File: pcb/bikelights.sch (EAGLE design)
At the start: 8 parts, among them J1 COMPUTER-PERIPHERAL-POWERRA

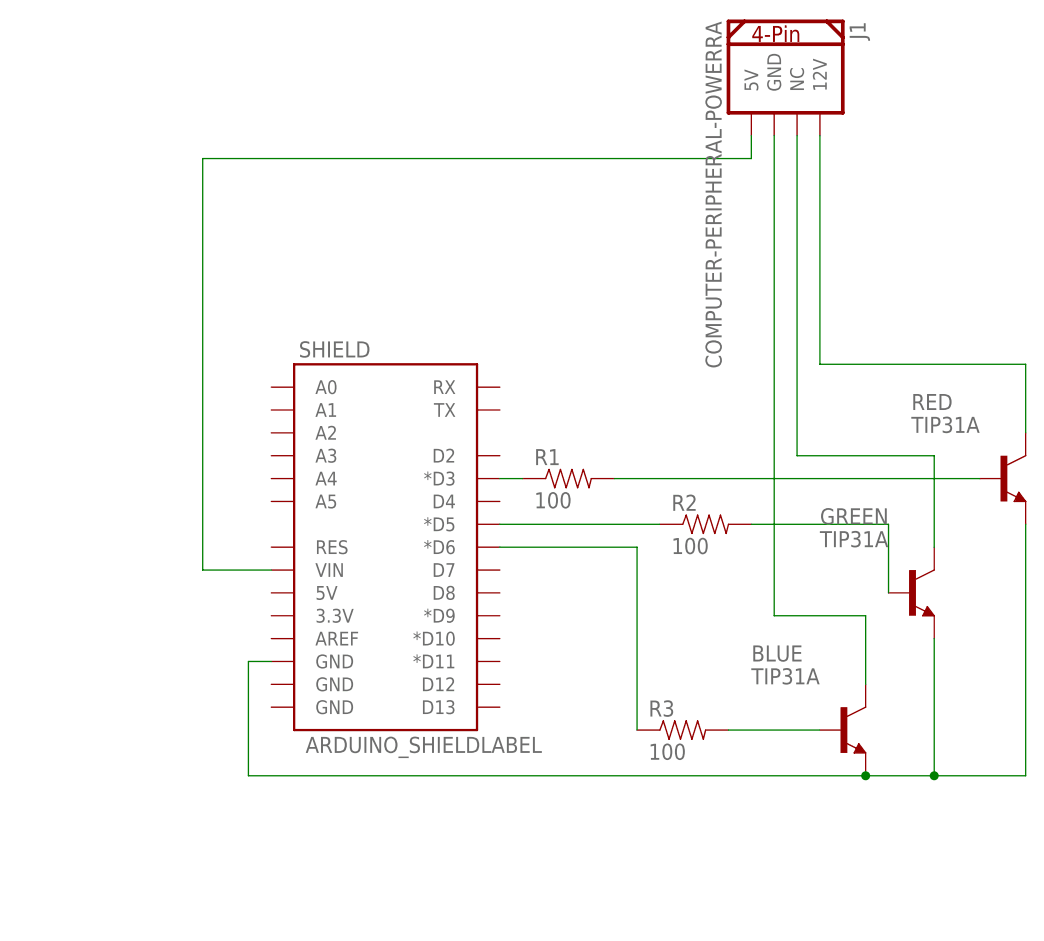
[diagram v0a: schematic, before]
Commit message: New PCB for blinkenthing B.
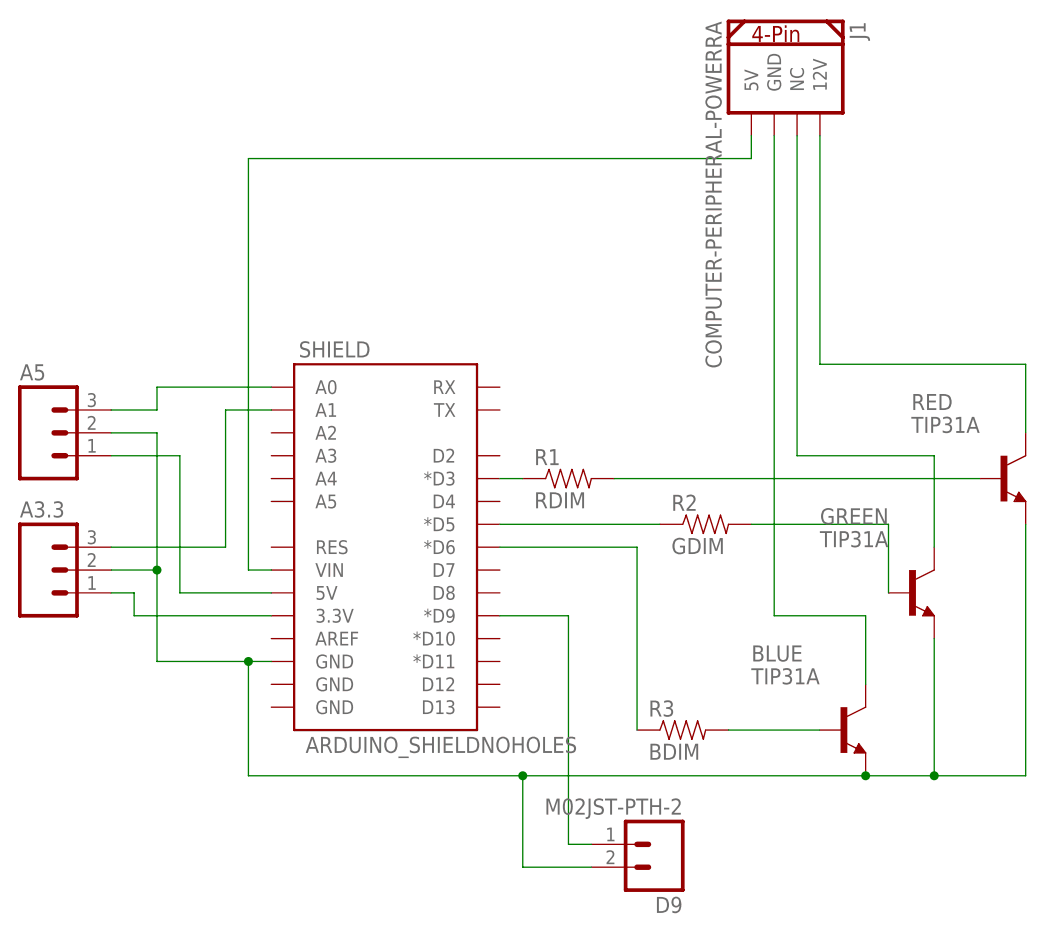
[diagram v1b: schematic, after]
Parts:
- added A3.3, A5: (no value), SparkFun-Connectors:M03JST-PTH
- added D9: M02JST-PTH-2, SparkFun-Connectors:M02JST-PTH-2
- R1: value 100 -> RDIM
- R2: value 100 -> GDIM
- R3: value 100 -> BDIM
- SHIELD: value ARDUINO_SHIELDLABEL -> ARDUINO_SHIELDNOHOLES; device SparkFun-Boards:ARDUINO_SHIELDLABEL -> SparkFun-Boards:ARDUINO_SHIELDNOHOLES
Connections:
- new net N$12: A5.1, SHIELD.5V
- new net N$13: D9.1, SHIELD.*D9
- new net N$14: A5.3, SHIELD.A0
- new net N$15: A3.3.3, SHIELD.A1
- new net N$16: A3.3.1, SHIELD.3.3V
- net N$4: now also A3.3.2, A5.2, D9.2
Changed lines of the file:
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@@
 <?xml version="1.0" encoding="utf-8"?>
 <!DOCTYPE eagle SYSTEM "eagle.dtd">
-<eagle version="6.5.0">
+<eagle version="6.4">
 <drawing>
 <settings>
@@
 <part name="GREEN" library="transistor" deviceset="TIP31" device="" technology="A"/>
 <part name="BLUE" library="transistor" deviceset="TIP31" device="" technology="A"/>
-<part name="SHIELD" library="SparkFun-Boards" deviceset="ARDUINO_SHIELD" device="LABEL"/>
+<part name="SHIELD" library="SparkFun-Boards" deviceset="ARDUINO_SHIELD" device="NOHOLES" value="ARDUINO_SHIELDNOHOLES"/>
 <part name="J1" library="SparkFun-Connectors" deviceset="COMPUTER-PERIPHERAL-POWER" device="RA"/>
-<part name="R1" library="SparkFun-Passives" deviceset="RESISTOR" device="EZ" value="100"/>
-<part name="R2" library="SparkFun-Passives" deviceset="RESISTOR" device="EZ" value="100"/>
-<part name="R3" library="SparkFun-Passives" deviceset="RESISTOR" device="EZ" value="100"/>
+<part name="R1" library="SparkFun-Passives" deviceset="RESISTOR" device="EZ" value="RDIM"/>
+<part name="R2" library="SparkFun-Passives" deviceset="RESISTOR" device="EZ" value="GDIM"/>
+<part name="R3" library="SparkFun-Passives" deviceset="RESISTOR" device="EZ" value="BDIM"/>
+<part name="D9" library="SparkFun-Connectors" deviceset="M02" device="JST-PTH-2"/>
+<part name="A5" library="SparkFun-Connectors" deviceset="M03" device="JST-PTH"/>
+<part name="A3.3" library="SparkFun-Connectors" deviceset="M03" device="JST-PTH"/>
 </parts>
 <sheets>
@@
 <instance part="R2" gate="G$1" x="73.66" y="40.64"/>
 <instance part="R3" gate="G$1" x="71.12" y="17.78"/>
+<instance part="D9" gate="G$1" x="68.58" y="5.08" rot="R180"/>
+<instance part="A5" gate="G$1" x="0" y="50.8"/>
+<instance part="A3.3" gate="G$1" x="0" y="35.56"/>
 </instances>
 <busses>
@@
 <wire x1="109.22" y1="40.64" x2="109.22" y2="12.7" width="0.1524" layer="91"/>
 <junction x="99.06" y="12.7"/>
-<wire x1="22.86" y1="12.7" x2="91.44" y2="12.7" width="0.1524" layer="91"/>
+<wire x1="22.86" y1="12.7" x2="53.34" y2="12.7" width="0.1524" layer="91"/>
 <junction x="91.44" y="12.7"/>
+<wire x1="53.34" y1="12.7" x2="91.44" y2="12.7" width="0.1524" layer="91"/>
 <wire x1="22.86" y1="12.7" x2="22.86" y2="25.4" width="0.1524" layer="91"/>
 <pinref part="SHIELD" gate="G$1" pin="GND@2"/>
+<pinref part="A5" gate="G$1" pin="2"/>
+<wire x1="7.62" y1="50.8" x2="12.7" y2="50.8" width="0.1524" layer="91"/>
+<wire x1="12.7" y1="50.8" x2="12.7" y2="35.56" width="0.1524" layer="91"/>
+<wire x1="12.7" y1="35.56" x2="12.7" y2="25.4" width="0.1524" layer="91"/>
+<wire x1="12.7" y1="25.4" x2="22.86" y2="25.4" width="0.1524" layer="91"/>
+<pinref part="A3.3" gate="G$1" pin="2"/>
 <wire x1="22.86" y1="25.4" x2="25.4" y2="25.4" width="0.1524" layer="91"/>
+<wire x1="7.62" y1="35.56" x2="12.7" y2="35.56" width="0.1524" layer="91"/>
+<junction x="12.7" y="35.56"/>
+<junction x="22.86" y="25.4"/>
+<pinref part="D9" gate="G$1" pin="2"/>
+<wire x1="60.96" y1="2.54" x2="53.34" y2="2.54" width="0.1524" layer="91"/>
+<wire x1="53.34" y1="2.54" x2="53.34" y2="12.7" width="0.1524" layer="91"/>
+<junction x="53.34" y="12.7"/>
 </segment>
 </net>
@@
 <segment>
 <pinref part="SHIELD" gate="G$1" pin="VIN"/>
-<wire x1="25.4" y1="35.56" x2="17.78" y2="35.56" width="0.1524" layer="91"/>
-<wire x1="17.78" y1="35.56" x2="17.78" y2="81.28" width="0.1524" layer="91"/>
-<wire x1="17.78" y1="81.28" x2="78.74" y2="81.28" width="0.1524" layer="91"/>
+<wire x1="25.4" y1="35.56" x2="22.86" y2="35.56" width="0.1524" layer="91"/>
+<wire x1="22.86" y1="35.56" x2="22.86" y2="81.28" width="0.1524" layer="91"/>
+<wire x1="22.86" y1="81.28" x2="78.74" y2="81.28" width="0.1524" layer="91"/>
 <pinref part="J1" gate="G$1" pin="5V"/>
 <wire x1="78.74" y1="81.28" x2="78.74" y2="83.82" width="0.1524" layer="91"/>
@@
 </segment>
 </net>
+<net name="N$12" class="0">
+<segment>
+<pinref part="A5" gate="G$1" pin="1"/>
+<wire x1="7.62" y1="48.26" x2="15.24" y2="48.26" width="0.1524" layer="91"/>
+<wire x1="15.24" y1="48.26" x2="15.24" y2="33.02" width="0.1524" layer="91"/>
+<pinref part="SHIELD" gate="G$1" pin="5V"/>
+<wire x1="15.24" y1="33.02" x2="25.4" y2="33.02" width="0.1524" layer="91"/>
+</segment>
+</net>
+<net name="N$14" class="0">
+<segment>
+<pinref part="A5" gate="G$1" pin="3"/>
+<wire x1="7.62" y1="53.34" x2="12.7" y2="53.34" width="0.1524" layer="91"/>
+<wire x1="12.7" y1="53.34" x2="12.7" y2="55.88" width="0.1524" layer="91"/>
+<pinref part="SHIELD" gate="G$1" pin="A0"/>
+<wire x1="12.7" y1="55.88" x2="25.4" y2="55.88" width="0.1524" layer="91"/>
+</segment>
+</net>
+<net name="N$15" class="0">
+<segment>
+<pinref part="A3.3" gate="G$1" pin="3"/>
+<wire x1="7.62" y1="38.1" x2="20.32" y2="38.1" width="0.1524" layer="91"/>
+<wire x1="20.32" y1="38.1" x2="20.32" y2="53.34" width="0.1524" layer="91"/>
+<pinref part="SHIELD" gate="G$1" pin="A1"/>
+<wire x1="20.32" y1="53.34" x2="25.4" y2="53.34" width="0.1524" layer="91"/>
+</segment>
+</net>
+<net name="N$16" class="0">
+<segment>
+<pinref part="A3.3" gate="G$1" pin="1"/>
+<wire x1="7.62" y1="33.02" x2="10.16" y2="33.02" width="0.1524" layer="91"/>
+<wire x1="10.16" y1="33.02" x2="10.16" y2="30.48" width="0.1524" layer="91"/>
+<pinref part="SHIELD" gate="G$1" pin="3.3V"/>
+<wire x1="10.16" y1="30.48" x2="25.4" y2="30.48" width="0.1524" layer="91"/>
+</segment>
+</net>
+<net name="N$13" class="0">
+<segment>
+<pinref part="SHIELD" gate="G$1" pin="*D9"/>
+<wire x1="50.8" y1="30.48" x2="58.42" y2="30.48" width="0.1524" layer="91"/>
+<wire x1="58.42" y1="30.48" x2="58.42" y2="5.08" width="0.1524" layer="91"/>
+<pinref part="D9" gate="G$1" pin="1"/>
+<wire x1="58.42" y1="5.08" x2="60.96" y2="5.08" width="0.1524" layer="91"/>
+</segment>
+</net>
 </nets>
 </sheet>
 </sheets>
+<errors>
+</errors>
 </schematic>
 </drawing>
